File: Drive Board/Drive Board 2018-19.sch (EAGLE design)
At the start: 77 parts, among them IC1 ACS758KCB, IC2 ACS758KCB, IC3 ACS758KCB, IC4 ACS758KCB, IC5 7812T, IC6 LM741P, K1 G5L, K2 G5L, K3 G5L

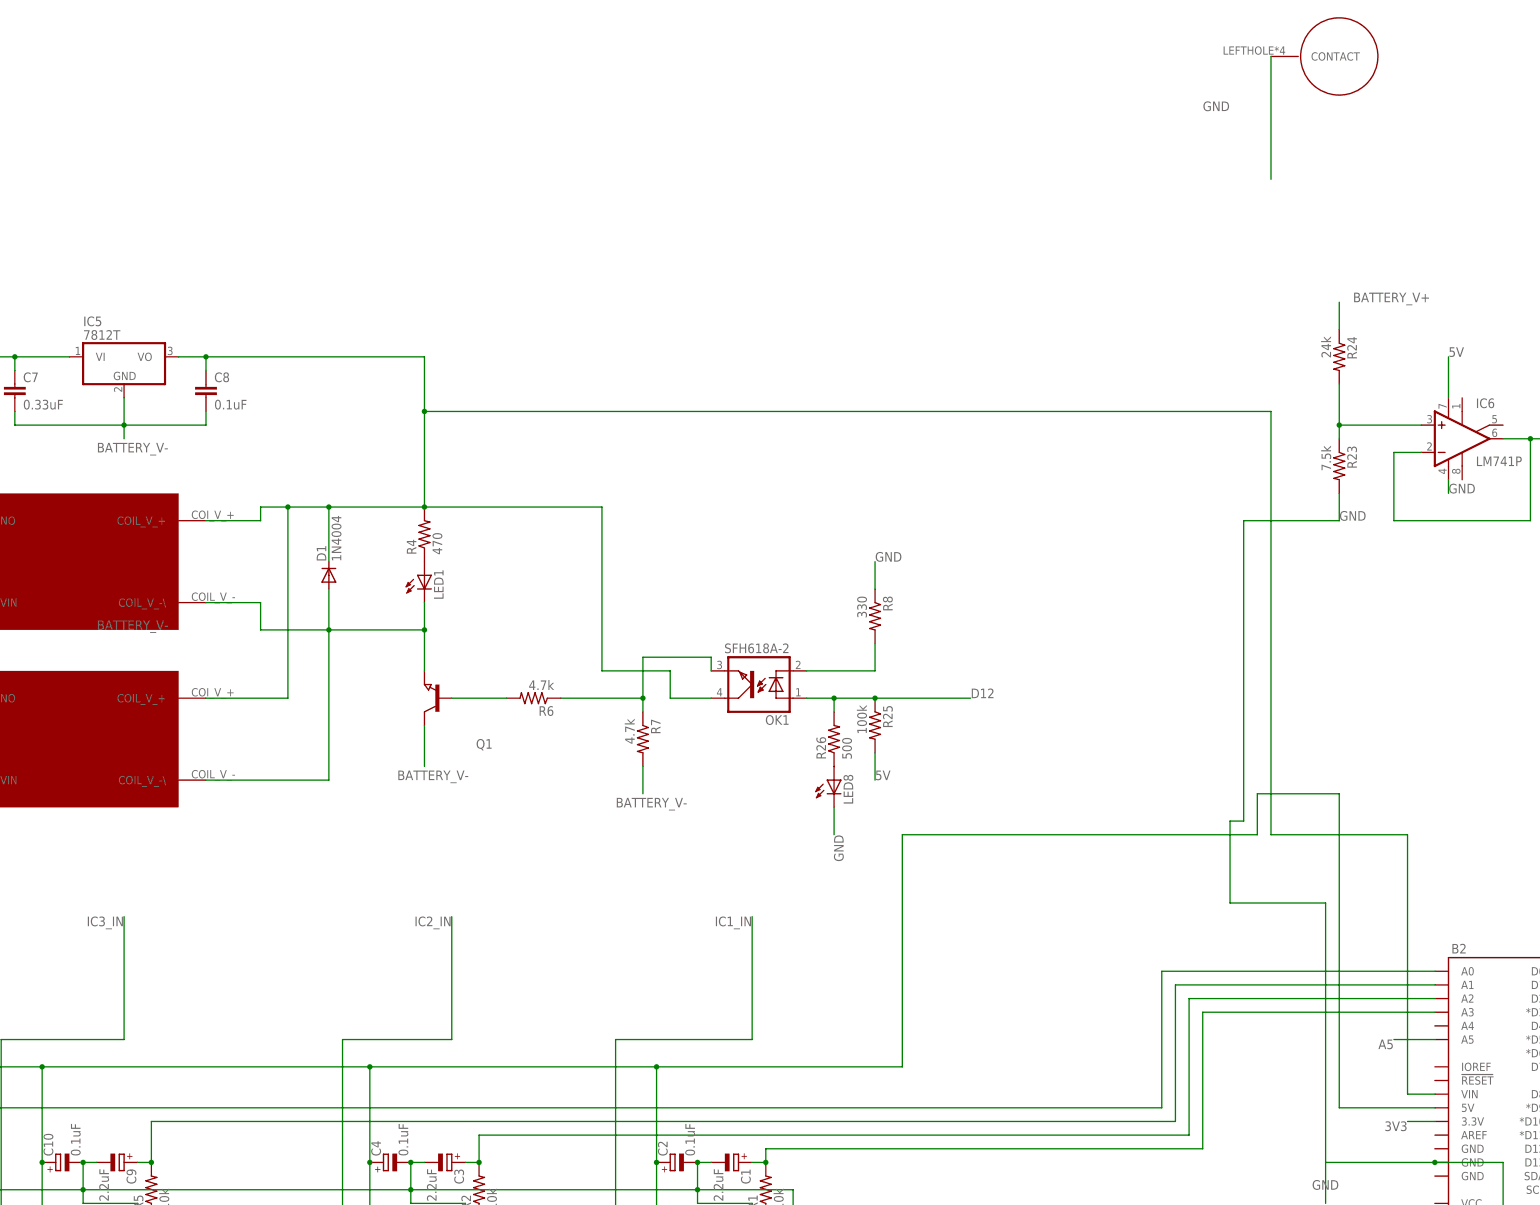
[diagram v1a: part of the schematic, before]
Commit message: fixed mixed ground network
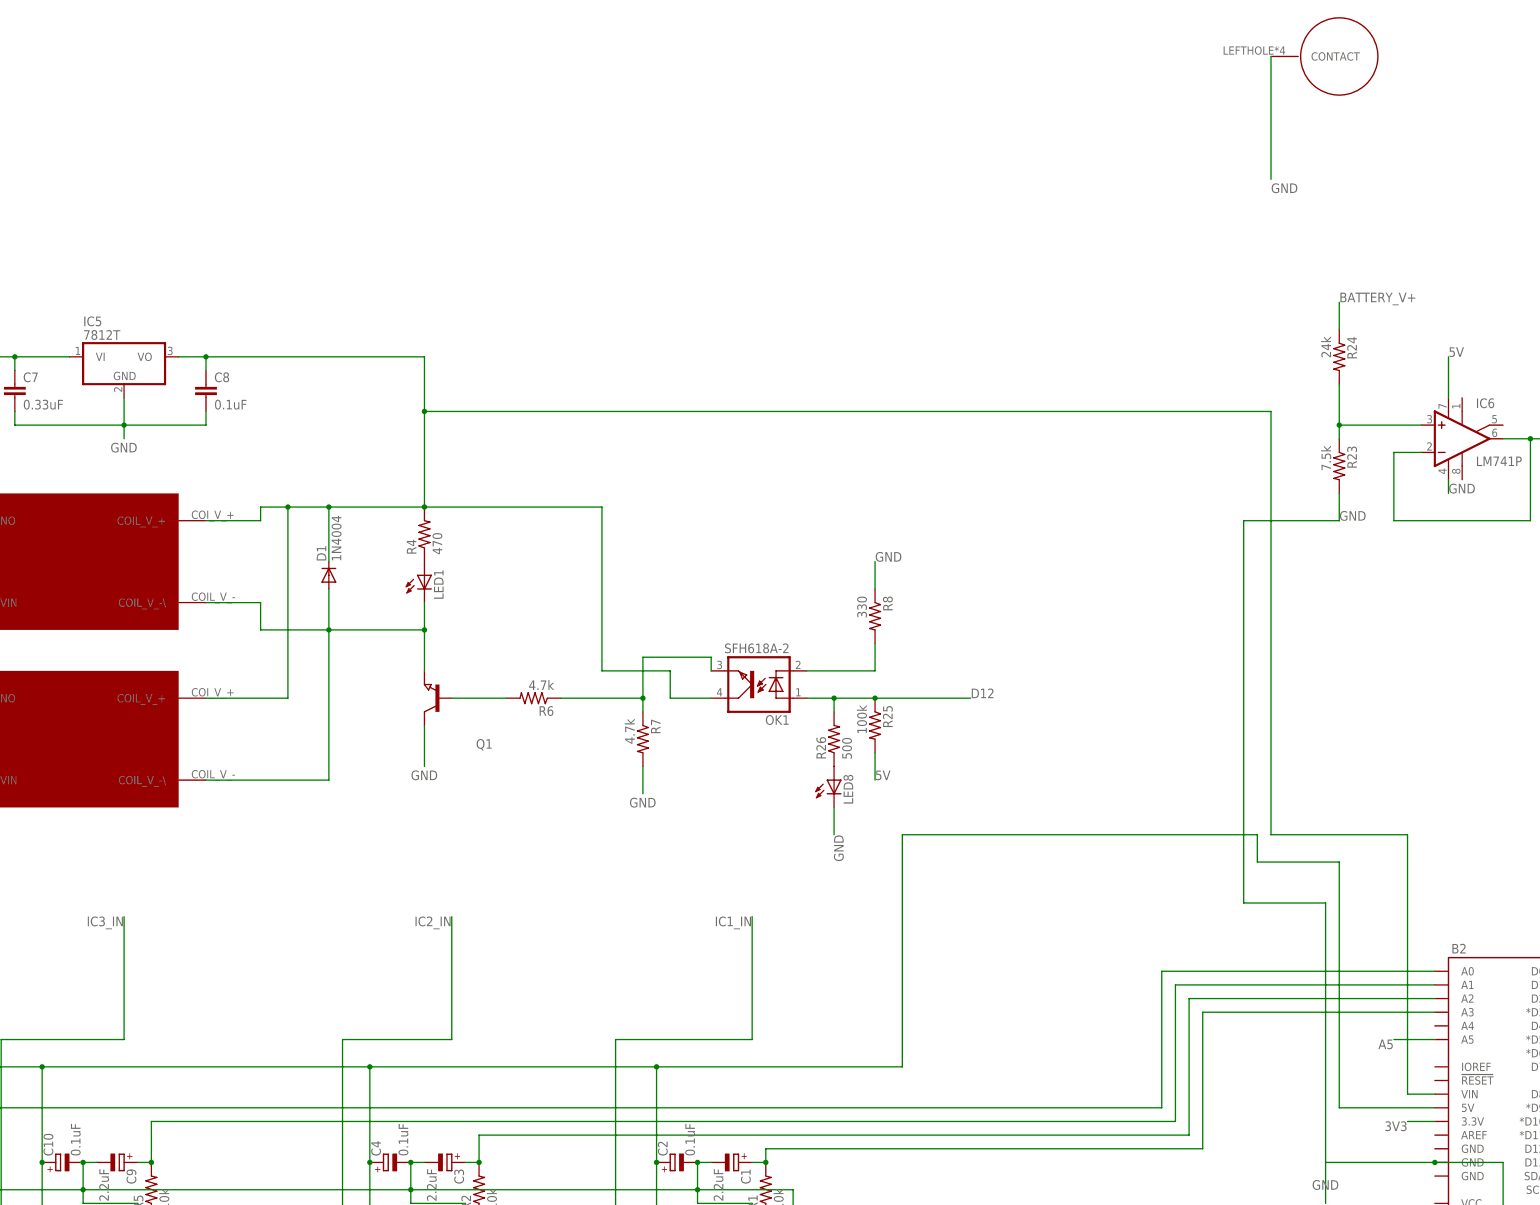
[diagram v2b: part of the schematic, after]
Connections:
- removed net BATTERY_V-: C7.2, C8.2, IC5.GND, Q1.C, R7.2
- net GND: now also C7.2, C8.2, IC5.GND, Q1.C, R7.2
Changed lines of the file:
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@@
 <junction x="-223.52" y="53.34"/>
 <junction x="-170.18" y="53.34"/>
-<wire x1="-58.42" y1="114.3" x2="-58.42" y2="121.92" width="0.1524" layer="91"/>
+<wire x1="-58.42" y1="114.3" x2="-58.42" y2="109.22" width="0.1524" layer="91"/>
 <pinref part="B2" gate="G$1" pin="5V"/>
 <wire x1="-25.4" y1="63.5" x2="-43.18" y2="63.5" width="0.1524" layer="91"/>
-<wire x1="-43.18" y1="63.5" x2="-43.18" y2="121.92" width="0.1524" layer="91"/>
-<wire x1="-58.42" y1="121.92" x2="-43.18" y2="121.92" width="0.1524" layer="91"/>
+<wire x1="-43.18" y1="63.5" x2="-43.18" y2="109.22" width="0.1524" layer="91"/>
+<wire x1="-58.42" y1="109.22" x2="-43.18" y2="109.22" width="0.1524" layer="91"/>
 </segment>
 <segment>
@@
 <pinref part="R24" gate="G$1" pin="1"/>
 <wire x1="-43.18" y1="208.28" x2="-43.18" y2="213.36" width="0.1524" layer="91"/>
-<label x="-40.64" y="213.36" size="1.778" layer="95"/>
+<label x="-43.18" y="213.36" size="1.778" layer="95"/>
 </segment>
 <segment>
@@
 <wire x1="-299.72" y1="124.46" x2="-304.8" y2="124.46" width="0.1524" layer="91"/>
 <label x="-302.26" y="124.46" size="1.778" layer="95" rot="R180"/>
-</segment>
-</net>
-<net name="BATTERY_V-" class="0">
-<segment>
-<pinref part="Q1" gate="G$1" pin="C"/>
-<wire x1="-213.36" y1="134.62" x2="-213.36" y2="127" width="0.1524" layer="91"/>
-<label x="-218.44" y="124.46" size="1.778" layer="95"/>
-</segment>
-<segment>
-<pinref part="R7" gate="G$1" pin="2"/>
-<wire x1="-172.72" y1="127" x2="-172.72" y2="121.92" width="0.1524" layer="91"/>
-<label x="-177.8" y="119.38" size="1.778" layer="95"/>
-</segment>
-<segment>
-<pinref part="IC5" gate="A1" pin="GND"/>
-<wire x1="-269.24" y1="195.58" x2="-269.24" y2="190.5" width="0.1524" layer="91"/>
-<pinref part="C7" gate="G$1" pin="2"/>
-<wire x1="-269.24" y1="190.5" x2="-289.56" y2="190.5" width="0.1524" layer="91"/>
-<wire x1="-289.56" y1="190.5" x2="-289.56" y2="193.04" width="0.1524" layer="91"/>
-<pinref part="C8" gate="G$1" pin="2"/>
-<wire x1="-269.24" y1="190.5" x2="-254" y2="190.5" width="0.1524" layer="91"/>
-<wire x1="-254" y1="190.5" x2="-254" y2="193.04" width="0.1524" layer="91"/>
-<junction x="-269.24" y="190.5"/>
-<wire x1="-269.24" y1="190.5" x2="-269.24" y2="187.96" width="0.1524" layer="91"/>
-<label x="-274.32" y="185.42" size="1.778" layer="95"/>
-</segment>
-<segment>
-<label x="-274.32" y="152.4" size="1.778" layer="95"/>
 </segment>
 </net>
@@
 <wire x1="-10.16" y1="30.48" x2="-12.7" y2="30.48" width="0.1524" layer="91"/>
 <wire x1="-12.7" y1="30.48" x2="-12.7" y2="53.34" width="0.1524" layer="91"/>
-<wire x1="-63.5" y1="116.84" x2="-60.96" y2="116.84" width="0.1524" layer="91"/>
 <wire x1="-45.72" y1="53.34" x2="-45.72" y2="101.6" width="0.1524" layer="91"/>
-<wire x1="-45.72" y1="101.6" x2="-63.5" y2="101.6" width="0.1524" layer="91"/>
-<wire x1="-63.5" y1="101.6" x2="-63.5" y2="116.84" width="0.1524" layer="91"/>
+<wire x1="-45.72" y1="101.6" x2="-60.96" y2="101.6" width="0.1524" layer="91"/>
 <pinref part="B2" gate="G$1" pin="GND@1"/>
 <wire x1="-12.7" y1="53.34" x2="-25.4" y2="53.34" width="0.1524" layer="91"/>
@@
 <wire x1="-45.72" y1="53.34" x2="-45.72" y2="45.72" width="0.1524" layer="91"/>
 <label x="-48.26" y="48.26" size="1.778" layer="95"/>
-<wire x1="-60.96" y1="116.84" x2="-60.96" y2="172.72" width="0.1524" layer="91"/>
+<wire x1="-60.96" y1="101.6" x2="-60.96" y2="172.72" width="0.1524" layer="91"/>
 <pinref part="R23" gate="G$1" pin="2"/>
 <wire x1="-43.18" y1="177.8" x2="-43.18" y2="172.72" width="0.1524" layer="91"/>
@@
 <pinref part="U$9" gate="G$1" pin="CONTACT"/>
 <wire x1="-55.88" y1="259.08" x2="-55.88" y2="236.22" width="0.1524" layer="91"/>
-<label x="-68.58" y="248.92" size="1.778" layer="95"/>
+<label x="-55.88" y="233.68" size="1.778" layer="95"/>
 </segment>
 <segment>
@@
 <label x="-137.16" y="114.3" size="1.778" layer="95" rot="R270"/>
 </segment>
-</net>
+<segment>
+<pinref part="IC5" gate="A1" pin="GND"/>
+<wire x1="-269.24" y1="195.58" x2="-269.24" y2="190.5" width="0.1524" layer="91"/>
+<pinref part="C7" gate="G$1" pin="2"/>
+<wire x1="-269.24" y1="190.5" x2="-289.56" y2="190.5" width="0.1524" layer="91"/>
+<wire x1="-289.56" y1="190.5" x2="-289.56" y2="193.04" width="0.1524" layer="91"/>
+<pinref part="C8" gate="G$1" pin="2"/>
+<wire x1="-269.24" y1="190.5" x2="-254" y2="190.5" width="0.1524" layer="91"/>
+<wire x1="-254" y1="190.5" x2="-254" y2="193.04" width="0.1524" layer="91"/>
+<junction x="-269.24" y="190.5"/>
+<wire x1="-269.24" y1="190.5" x2="-269.24" y2="187.96" width="0.1524" layer="91"/>
+<label x="-271.78" y="185.42" size="1.778" layer="95"/>
+</segment>
+<segment>
+<pinref part="Q1" gate="G$1" pin="C"/>
+<wire x1="-213.36" y1="134.62" x2="-213.36" y2="127" width="0.1524" layer="91"/>
+<label x="-215.9" y="124.46" size="1.778" layer="95"/>
+</segment>
+<segment>
+<pinref part="R7" gate="G$1" pin="2"/>
+<wire x1="-172.72" y1="127" x2="-172.72" y2="121.92" width="0.1524" layer="91"/>
+<label x="-175.26" y="119.38" size="1.778" layer="95"/>
+</segment>
+</net>

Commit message: Added Components for relay
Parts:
- removed U$8: JTN1AS-PA-F-DC12V, RSX_driver_relay:JTN1AS-PA-F-DC12V
- added D2, D3, D4: 1N4004, diode:1N4004
- added LED10, LED11, LED12, LED13, LED14, LED9: (no value), eagle-ltspice:LED_E
- added OK2, OK3, OK4: SFH618A-2, optocoupler:SFH618A-2
- added Q2, Q3, Q4: (no value), semicon-smd-ipc:NPN-TRANSISTOR_SOT23
- added R27, R33, R39: 470, resistor:R-US_0207/10
- added R28, R29, R34, R35, R40, R41: 4.7k, resistor:R-US_0207/10
- added R30, R36, R42: 330, resistor:R-US_0207/10
- added R31, R37, R43: 100k, resistor:R-US_0207/10
- added R32, R38, R44: 500, resistor:R-US_0207/10
- added S1, S10, S2, S9: (no value), switch-dil:DS01E
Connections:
- removed net COIL_V+: B2.VIN, C8.1, D1.C, IC5.VO, K11.2, K21.2, K31.2, OK1.COL, R4.2, U$11.COIL_V_+, U$8.COIL_V_+
- removed net COIL_V-: D1.A, K11.1, K21.1, K31.1, LED1.C, Q1.E, U$11.COIL_V_-\, U$8.COIL_V_-\
- new net COIL_V-_1: D1.A, LED1.C, Q1.E, U$11.COIL_V_-\
- new net COIL_V-_2: D2.A, K31.1, LED9.C, Q2.E
- new net COIL_V-_3: D3.A, K21.1, LED11.C, Q3.E
- new net COIL_V-_4: D4.A, K11.1, LED13.C, Q4.E
- new net N$11: OK2.EMIT, R28.1, R29.1
- new net N$12: OK2.C, R30.2
- new net N$14: LED10.A, R32.1
- new net N$15: LED11.A, R33.1
- new net N$18: Q3.B, R34.2
- new net N$20: OK3.EMIT, R34.1, R35.1
- new net N$22: OK3.C, R36.2
- new net N$23: LED12.A, R38.1
- new net N$25: LED13.A, R39.1
- new net N$26: Q4.B, R40.2
- new net N$27: OK4.EMIT, R40.1, R41.1
- new net N$28: OK4.C, R42.2
- new net N$29: LED14.A, R44.1
- new net N$7: LED9.A, R27.1
- new net N$9: Q2.B, R28.2
- new net OPTO1: OK2.A, R31.1, R32.2, S9.1
- new net OPTO2: OK3.A, R37.1, R38.2, S2.1
- new net OPTO3: OK4.A, R43.1, R44.2, S1.1
- new net OPTO4: OK1.A, R25.1, R26.2, S10.1
- new net VOLTAGE_REG_OUT: B2.VIN, C8.1, D1.C, D2.C, D3.C, D4.C, IC5.VO, K11.2, K21.2, K31.2, OK1.COL, OK2.COL, OK3.COL, OK4.COL, R27.2, R33.2, R39.2, R4.2, U$11.COIL_V_+
- net 5V: now also S1.2, S10.2, S2.2, S9.2; no longer R25.2
- net BATTERY_V+: no longer U$8.VIN
- net D12: no longer OK1.A, R25.1, R26.2
- net GND: now also LED10.C, LED12.C, LED14.C, Q2.C, Q3.C, Q4.C, R25.2, R29.2, R30.1, R31.2, R35.2, R36.1, R37.2, R41.2, R42.1, R43.2
- net N$24: no longer U$8.NO
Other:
- moved on the sheet: K1, K2, K3

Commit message: Relay control from DIO pins implemented
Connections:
- new net A4: B2.A4, IC6.-IN, IC6.OUT
- net 5V: no longer S1.2, S2.2, S9.2
- net A5: now also S9.2; no longer IC6.-IN, IC6.OUT
- net D12: now also S1.2
- net D13: now also S2.2
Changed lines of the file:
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@@
-</segment>
-<segment>
-<pinref part="S9" gate="1" pin="2"/>
-<wire x1="-426.72" y1="195.58" x2="-416.56" y2="195.58" width="0.1524" layer="91"/>
-<label x="-416.56" y="195.58" size="1.778" layer="95"/>
-</segment>
-<segment>
-<pinref part="S2" gate="1" pin="2"/>
-<wire x1="-429.26" y1="93.98" x2="-416.56" y2="93.98" width="0.1524" layer="91"/>
-<label x="-416.56" y="93.98" size="1.778" layer="95"/>
-</segment>
-<segment>
-<pinref part="S1" gate="1" pin="2"/>
-<wire x1="-431.8" y1="7.62" x2="-421.64" y2="7.62" width="0.1524" layer="91"/>
-<label x="-421.64" y="7.62" size="1.778" layer="95"/>
 </segment>
 <segment>
@@
 <label x="7.62" y="55.88" size="1.778" layer="95"/>
 </segment>
+<segment>
+<pinref part="S1" gate="1" pin="2"/>
+<wire x1="-431.8" y1="7.62" x2="-421.64" y2="7.62" width="0.1524" layer="91"/>
+<label x="-421.64" y="7.62" size="1.778" layer="95"/>
+</segment>
 </net>
 <net name="D13" class="0">
@@
 <wire x1="0" y1="53.34" x2="7.62" y2="53.34" width="0.1524" layer="91"/>
 <label x="7.62" y="53.34" size="1.778" layer="95"/>
+</segment>
+<segment>
+<pinref part="S2" gate="1" pin="2"/>
+<wire x1="-429.26" y1="93.98" x2="-416.56" y2="93.98" width="0.1524" layer="91"/>
+<label x="-416.56" y="93.98" size="1.778" layer="95"/>
 </segment>
 </net>
@@
 </segment>
 <segment>
-<pinref part="IC6" gate="A" pin="-IN"/>
-<wire x1="-27.94" y1="185.42" x2="-33.02" y2="185.42" width="0.1524" layer="91"/>
-<wire x1="-33.02" y1="185.42" x2="-33.02" y2="172.72" width="0.1524" layer="91"/>
-<wire x1="-33.02" y1="172.72" x2="-7.62" y2="172.72" width="0.1524" layer="91"/>
-<wire x1="-7.62" y1="172.72" x2="-7.62" y2="187.96" width="0.1524" layer="91"/>
-<pinref part="IC6" gate="A" pin="OUT"/>
-<wire x1="-7.62" y1="187.96" x2="-12.7" y2="187.96" width="0.1524" layer="91"/>
-<wire x1="-7.62" y1="187.96" x2="2.54" y2="187.96" width="0.1524" layer="91"/>
-<junction x="-7.62" y="187.96"/>
-<label x="2.54" y="187.96" size="1.778" layer="95"/>
+<pinref part="S9" gate="1" pin="2"/>
+<wire x1="-426.72" y1="195.58" x2="-416.56" y2="195.58" width="0.1524" layer="91"/>
+<label x="-416.56" y="195.58" size="1.778" layer="95"/>
 </segment>
 </net>
@@
 </segment>
 </net>
+<net name="A4" class="0">
+<segment>
+<pinref part="B2" gate="G$1" pin="A4"/>
+<wire x1="-25.4" y1="78.74" x2="-33.02" y2="78.74" width="0.1524" layer="91"/>
+<label x="-33.02" y="78.74" size="1.778" layer="95" rot="R180"/>
+</segment>
+<segment>
+<pinref part="IC6" gate="A" pin="-IN"/>
+<wire x1="-27.94" y1="185.42" x2="-33.02" y2="185.42" width="0.1524" layer="91"/>
+<wire x1="-33.02" y1="185.42" x2="-33.02" y2="172.72" width="0.1524" layer="91"/>
+<wire x1="-33.02" y1="172.72" x2="-7.62" y2="172.72" width="0.1524" layer="91"/>
+<wire x1="-7.62" y1="172.72" x2="-7.62" y2="187.96" width="0.1524" layer="91"/>
+<pinref part="IC6" gate="A" pin="OUT"/>
+<wire x1="-7.62" y1="187.96" x2="-12.7" y2="187.96" width="0.1524" layer="91"/>
+<wire x1="-7.62" y1="187.96" x2="2.54" y2="187.96" width="0.1524" layer="91"/>
+<junction x="-7.62" y="187.96"/>
+<label x="2.54" y="187.96" size="1.778" layer="95"/>
+</segment>
+</net>
